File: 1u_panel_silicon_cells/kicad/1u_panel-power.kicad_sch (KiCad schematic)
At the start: 70 parts, among them J1 MMS-104-01-[F/L]-SH, Q1 DMP3050LVT-7, Q2 DMP2240UDM-7, U10 TPS63060DSCR, U12 LTC4412, U3 LT1618EMSTRPBF, U4 INA226

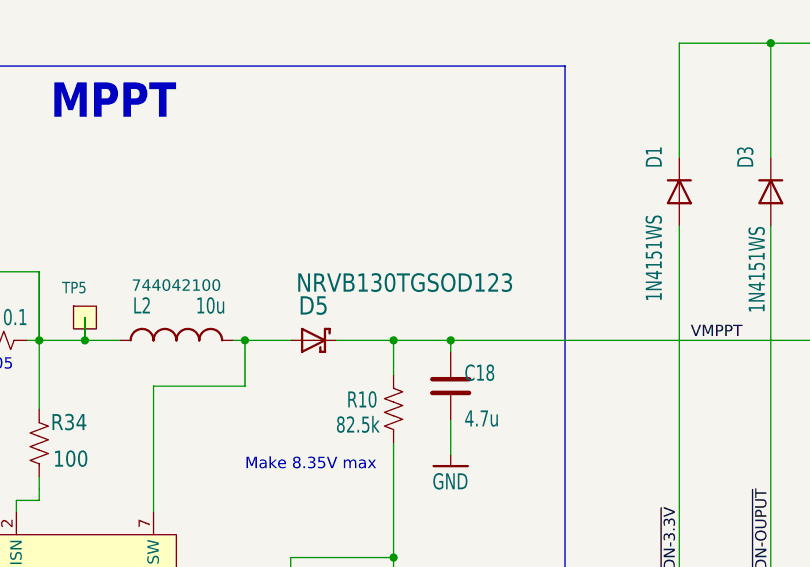
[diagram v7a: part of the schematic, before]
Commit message: updated part numbers for all components on silicon module to be flight-ready hardware PNs, pulled from CFC mfr series'
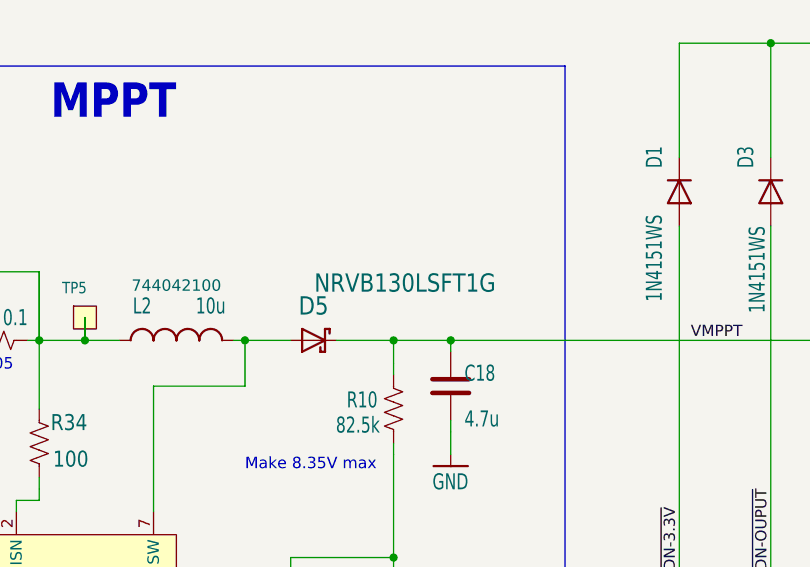
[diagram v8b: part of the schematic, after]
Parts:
- C12: DPN 490-10516-2-ND -> 490-GRT21BC71E106KE13LCT-ND; Distributor (none) -> Digi-Key; MFR Murata -> Murata Electronics; MPN GRM21BR71A106KA73L -> GRT21BC71E106KE13L
- C13, C20, C4: Distributor (none) -> Digi-Key; MFR Murata -> Murata Electronics
- C14, C18: DPN 490-GRM188Z71C475KE21JTR-ND -> 1276-1784-1-ND; Distributor (none) -> Digi-Key; MFR Murata -> Samsung Electro-Mechanics; MPN GRM188Z71C475KE21J -> CL10A475KO8NNNC
- C15, C19, C23: DPN 2571-GMC21X7R226M10NTTR-ND -> 490-GRT21BC81C226ME13KTR-ND; Distributor (none) -> Digi-Key; MFR Cal-Chip -> Murata; MPN GMC21X7R226M10NT -> GRT21BC81C226ME13K
- C2: DPN 490-4781-2-ND -> 399-14102-1-ND; Distributor (none) -> Digi-Key; MFR Murata -> KEMET; MPN GCM188R72A103KA37D -> C0603C103J3GECAUTO
- C21, C6, C7, C8: DPN 490-5798-2-ND -> 399-C0603C101J5GAC3190CT-ND; Distributor (none) -> Digi-Key; MFR Murata -> KEMET; MPN GCJ188R71H104KA12D -> C0603C101J5GAC3190
- C22: DPN 490-8011-2-ND -> 399-6840-1-ND; Distributor (none) -> Digi-Key; MFR Murata -> KEMET; MPN GCM1885G1H100JA16D -> C0603C100J5GACAUTO
- CF1, J1, L1, L2, R17, U4: Distributor (none) -> Digi-Key
- D1, D3: DPN 12-1N4151WS-E3-08TR-ND -> 112-1N4151WS-E3-08CT-ND; Distributor (none) -> Digi-Key; MPN 1N4151WS-E3-08 -> 1N4151WS-E3-08
- D4: DPN 1830-1064-1-ND -> 732-4971-1-ND; Distributor (none) -> Digi-Key; MFR Inolux -> Wurth; MPN IN-S63AT5A -> 150060GS75000
- D5: value NRVB130TGSOD123 -> NRVB130LSFT1G; DPN NRVB130T3GOSCT-ND -> NRVB130LSFT1GOSTR-ND; Distributor (none) -> Digi-Key; MPN NRVB130T3G -> NRVB130LSFT1G
- Q1, Q2: Distributor (none) -> Digi-Key; MFR Diodes Inc. -> Diodes Inc
- R1: DPN YAG4574TR-ND -> RMCF0603FT560KTR-ND; Distributor (none) -> Digi-Key; MFR Yaego -> Stackpole Electronics Inc; MPN RT0603BRD07560KL -> RMCF0603FT560K
- R10: DPN P82.5KDBCT-ND -> RMCF0603FT82K5TR-ND; Distributor (none) -> Digi-Key; MFR Panasonic -> Stackpole Electronics Inc; MPN ERA-3AEB8252V -> RMCF0603FT82K5
- R11: DPN RMCF0603JT10K0 -> RMCF0603FT10K0CT-ND; Distributor (none) -> Digi-Key; MFR Stackpole -> Stackpole Electronics Inc; MPN RMCF0603JT10K0 -> RMCF0603FT10K0
- R12: Distributor (none) -> Digi-Key; MFR Stackpole -> Stackpole Electronics Inc
- R13: DPN RNCP0603FTD10K0CT-ND -> RMCF0603FT10K0CT-ND; Distributor (none) -> Digi-Key; MFR Stackpole -> Stackpole Electronics Inc; MPN RNCP0603FTD10K0 -> RMCF0603FT10K0
- R14, R20: DPN RMCF0805ZT0R00CT-ND -> P0.0ATR-ND; Distributor (none) -> Digi-Key; MFR Stackpole -> Panasonic; MPN RMCF0805ZT0R00 -> ERJ-6GEY0R00V
- R16: DPN 2019-RK73H1JTTD2001FCT-ND -> RMCF0603FT2K00TR-ND; Distributor (none) -> Digi-Key; MFR KOA -> Stackpole Electronics Inc; MPN RK73H1JTTD2001F -> RMCF0603FT2K00
- R18, R19, R2, R6, R7: DPN RR08P100KDCT-ND -> RMCF0603FT100KCT-ND; Distributor (none) -> Digi-Key; MFR Susumu -> Stackpole Electronics Inc; MPN RR0816P-104-D -> RMCF0603FT100K
- R21: DPN A129693CT-ND -> RMCF0603FT2K70TR-ND; Distributor (none) -> Digi-Key; MFR TE -> Stackpole Electronics Inc; MPN CRGCQ0603F2K7 -> RMCF0603FT2K70
- R34, R35, R36, R37: DPN 311-100HRTR-ND -> RMCF0603FT100RTR-ND; Distributor (none) -> Digi-Key; MFR Yaego -> Stackpole Electronics Inc; MPN RC0603FR-07100RL -> RMCF0603FT100R
- R9: DPN 311-1.00MHRTR-ND -> RMCF0603FG1M00CT-ND; Distributor (none) -> Digi-Key; MFR Yaego -> Stackpole Electronics Inc; MPN RC0603FR-071ML -> RMCF0603FG1M00
- U10: Distributor (none) -> Digi-Key; MPN TPS63060DSCR -> IC REG BUCK BOOST ADJ 2A 10WSON
- U12: DPN LTC4412ES6#TRPBFCT-ND -> 505-LTC4412ES6#TRPBFTR-ND; Distributor (none) -> Digi-Key
- U3: DPN LT1618EMS#TRPBFCT-ND -> LT1618EMS#TRPBFTR-ND; Distributor (none) -> Digi-Key; MFR Linear Technologies -> Analog Devices Inc.; MPN LT1618EMS#TRPBF -> IC REG BOOST ADJ 1.5A 10MSOP
